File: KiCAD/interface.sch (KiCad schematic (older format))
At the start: 23 parts, among them M1 MANIFOLD, P10 C3SB, P11 VSel_Vlv, P14 X_VALVE, P17 PUMP, P18 Pump_Cable, P7 GAGE_PR, P9 C3SB, Q1 BCP5416TA, Q2 BCP5416TA, U1 TXB0104D

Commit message: work in progress
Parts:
- removed M1: MANIFOLD, symbol MANIFOLD
- added C14, C31: 100nF, uCm:c_0805, symbol C
- added D3, D9: S1D-13-F, uCm:diode-DO214AC, symbol D_1N4001
- added P34: VSel_Vlv2, uCm:Header_3, symbol CONN_3
- added P38: X_VALVE2, uCm:X_Valve_2, symbol X_VALVE
- added Q3, Q4: BCP5416TA, uCm:SOT223, symbol NPN_TIP112G
- added R6: 1k, uCm:r_0805, symbol R_10k
- added SP1: BUZZER, uCm:Speaker, symbol BUZZER
- C10, C11, C13, C17, C29, C7, C8, C9: footprint c_0805 -> uCm:c_0805
- C27: footprint C_ELCO_SMD -> uCm:C_ELCO_SMD
- D1: footprint diode-DO214AC -> uCm:diode-DO214AC
- P10, P9: footprint pin_strip_4-90 -> uCm:pin_strip_4-90
- P11: footprint Header_3 -> uCm:Header_3
- P14: footprint X_Valve_2 -> uCm:X_Valve_2
- P17: footprint Pump_P54E01R_02 -> uCm:Pump_P54E01R_02; symbol PUMP -> Pump
- P7: footprint HCEM500GUH9P3 -> uCm:HCEM500GUH9P3; symbol GAGE_PR -> Gage_Pr
- Q1, Q2: footprint SOT223 -> uCm:SOT223
- R4, R5: footprint r_0805 -> uCm:r_0805
- U1: footprint TXB0104D -> uCm:TXB0104D
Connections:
- net labels added: +Vlv2, -Vlv2, PD4_Valve2, Spk, ~PD6_Spk
- wire segments 100 -> 133
- no-connect marks 12 -> 8
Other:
- note added: "Speaker, 5V DC\ndigital PWM port ~PD6"
- note added: "Valve #2 on digital port PD4\neither 12V (V_IN) or 5V0"
- moved on the sheet: C13, D1, P11, P14, Q1

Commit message: layout, work in progress
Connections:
- net +Vlv: now also P14.2 (PM); no longer P14.1 (P1)
- net +Vlv2: now also P38.2 (PM); no longer P38.1 (P1)
- net -Vlv: now also P14.1 (P1); no longer P14.2 (PM)
- net -Vlv2: now also P38.1 (P1); no longer P38.2 (PM)
- net PD4_Valve2: now also Q1.1 (B); no longer Q3.1 (B)
- net ~PD5_Valve: now also Q3.1 (B); no longer Q1.1 (B)
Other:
- note added: "Valve #1 on digital port PD4\neither 12V (V_IN) or 5V0"
- note added: "Valve #2 on digital port PD5 [PWM]\neither 12V (V_IN) or 5V0"
- note removed: "Valve #1 on digital PWM port\neither 12V (V_IN) or 5V0"
- note removed: "Valve #2 on digital port PD4\neither 12V (V_IN) or 5V0"
- moved on the sheet: C13, C14, C31, D1, D3, D9, P11, P14, P34, P38, Q1, Q3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

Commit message: layout, work in progress
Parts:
- removed P17: PUMP, uCm:Pump_P54E01R_02, symbol Pump
- added P17: PUMP, uCm:Pump_P54E01R_02, symbol CONN_5
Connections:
- net 12V: now also P17.2
- net Pump: now also P17.4
- net Pump_Ret: now reaches C17.2, C27.2 (-), C29.2, Q2.2 (C)
- net Pump_Ret: now also P17.1
- no-connect marks 8 -> 7
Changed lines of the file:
@@
-$EndComp
-$Comp
-L Pump P17
-U 1 1 50E2B32E
-P 4600 5600
-F 0 "P17" V 4550 5600 40  0000 C CNN
-F 1 "PUMP" V 4650 5600 40  0000 C CNN
-F 2 "uCm:Pump_P54E01R_02" V 4750 5600 60  0001 C CNN
-F 3 "" H 4600 5600 60  0001 C CNN
-F 4 "http://www.xavitech.com/products" H 4600 6400 60  0001 L CNN "Field11"
-	1    4600 5600
-	1    0    0    -1
 $EndComp
 $Comp
@@
 	4000 5650 4000 6275
 NoConn ~ 4250 5750
-NoConn ~ 4250 5850
 Wire Notes Line
 	5575 7100 5575 5200
@@
 Text HLabel 8900 1200 0    40   Input ~ 0
 SDA
+Text Label 3250 6925 0    40   ~ 0
+Pump_Ret
+$Comp
+L CONN_5 P17
+U 1 1 55E98293
+P 4600 5550
+F 0 "P17" V 4550 5550 40  0000 C CNN
+F 1 "PUMP" V 4650 5550 40  0000 C CNN
+F 2 "uCm:Pump_P54E01R_02" H 4600 5500 60  0001 C CNN
+F 3 "http://www.xavitech.com/products" H 4600 5500 60  0001 C CNN
+	1    4600 5550
+	1    0    0    -1
+$EndComp
 $EndSCHEMATC

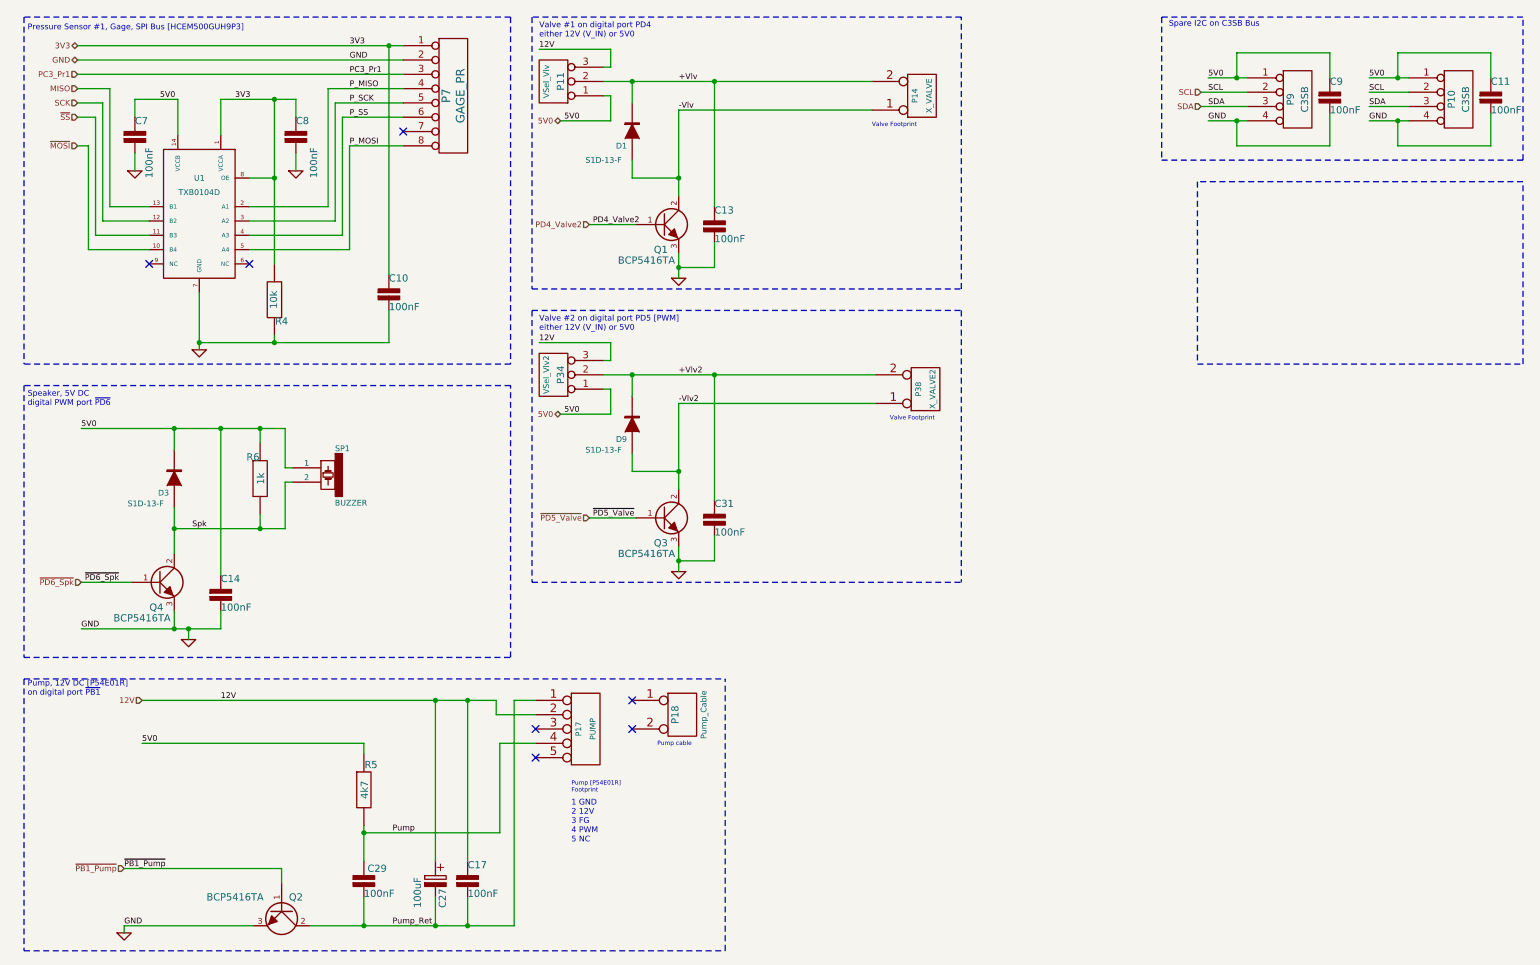
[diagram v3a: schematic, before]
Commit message: changed power supply section
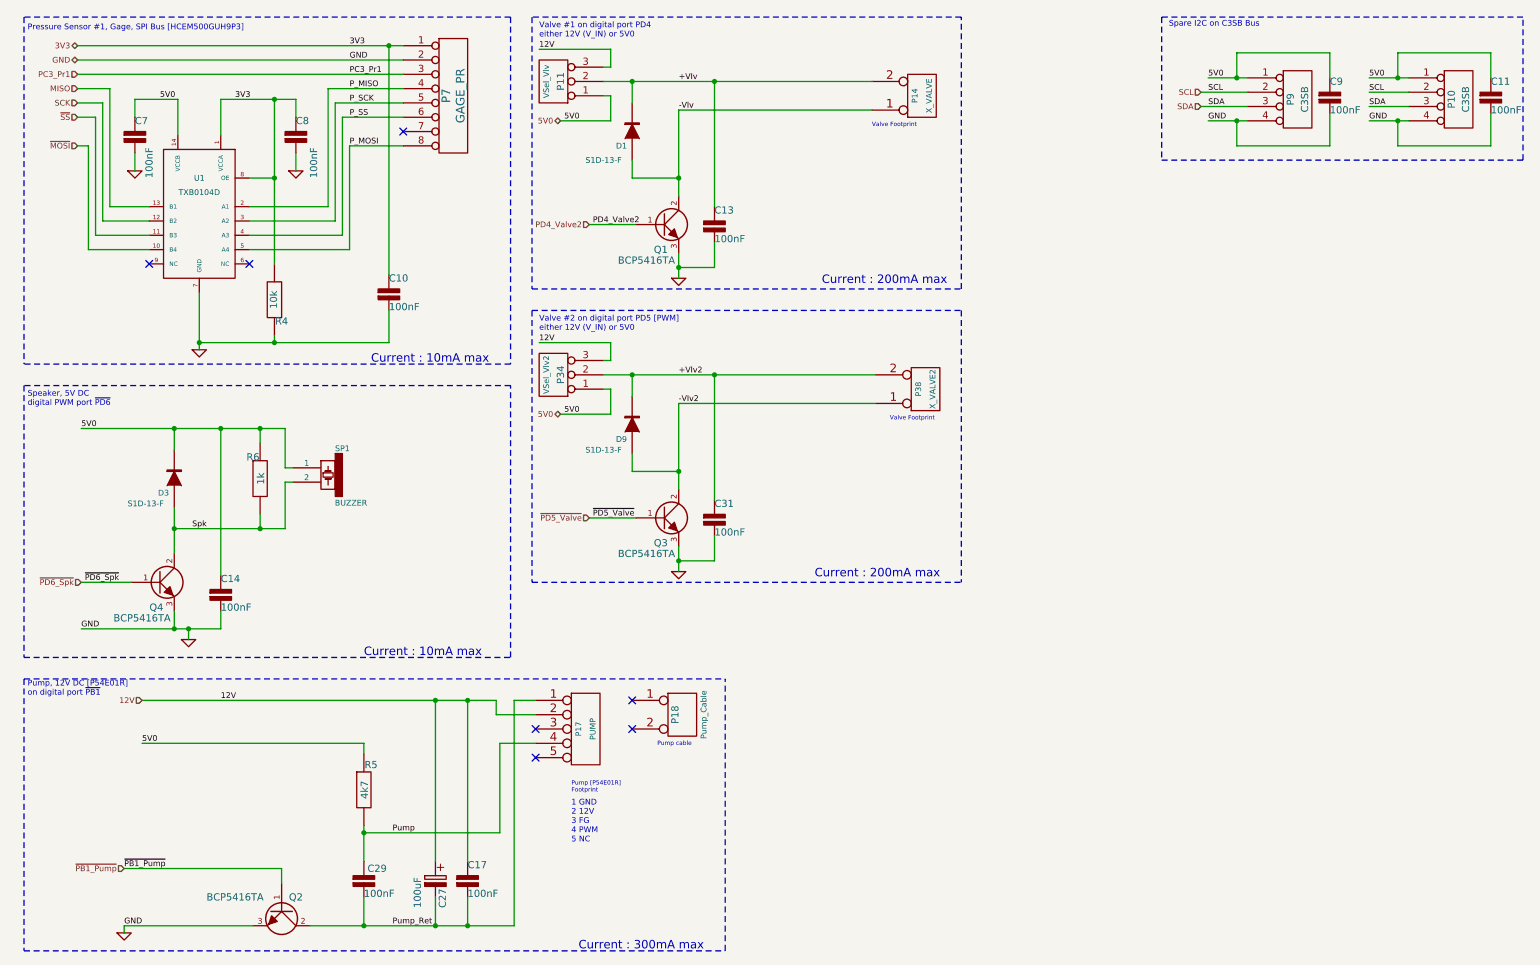
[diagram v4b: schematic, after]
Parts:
- C10, C11, C13, C14, C17, C29, C31, C7, C8, C9: Field10 399-5863-ND -> (none); Field11 http://www.digikey.com/product-detail/en/R82DC3100AA50J/399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 -> (none); Field4 CAP FILM 0.1UF 63VDC RADIAL -> (none); Field5 100nF, 63V -> (none); Field6 R82 -> (none); Field7 Kemet -> (none); Field8 R82DC3100AA50J -> (none); Field9 Digikey -> (none); manf# (none) -> CL21B104KCC5PNC
- C27: Field10 P833-ND -> (none); Field11 http://www.digikey.com/product-detail/en/ECE-A1CKA101/P833-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 -> (none); Field4 CAP ALUM 100UF 16V 20% RADIAL -> (none); Field5 100u,16V -> (none); Field6 Radial, Can, 6.3mm dia -> (none); Field7 Panasonic Electronic Components -> (none); Field8 ECE-A1CKA101 -> (none); Field9 Digikey -> (none); manf# (none) -> UWT1V101MCL1GS
- D1, D3, D9: Field10 1N4001FSCT-ND -> (none); Field11 http://www.digikey.com/product-detail/en/1N4001/1N4001FSCT-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 -> (none); Field4 DIODE GEN PURPOSE 50V 1A DO41 -> (none); Field5 50V, 1A -> (none); Field6 DO-204AL, DO-41, Axial -> (none); Field7 Fairchild Semiconductor -> (none); Field8 1N4001 -> (none); Field9 Digikey -> (none); manf# (none) -> S1D-13-F
- P10: manf# (none) -> PREC004SAAN-RC
- P11, P34: manf# (none) -> PREC003SAAN-RC
- P14, P38: Field10 X-1-05-S-F -> (none); Field11 http://ph.parker.com/webapp/wcs/stores/servlet/Product2_101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 -> (none); Field4 Miniature Pneumatic Solenoid Valve -> (none); Field5 3 Port, Direct-acting poppet style -> (none); Field6 8mm Solenoid Valve -> (none); Field7 Parker Hannifin Corporation -> (none); Field8 X-1-05-S-F -> (none); Field9 Parker Hannifin Corporation -> (none); manf# (none) -> X-1-05-S-F
- P17: manf# (none) -> P54E01R
- P7: Field10 HCEM500GUH9P3 -> (none); Field11 http://www.sensortechnics.com/en/products/pressure-sensors-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 -> (none); Field4 Miniature amplified pressure sensor -> (none); Field5 HCE Series -> (none); Field6 SMD single port, barbed port -> (none); Field7 SensorTechnics -> (none); Field8 HCEM500GUH9P3 -> (none); Field9 SensorTechnics -> (none); manf# (none) -> HCEM500GUH9P3
- P9: Field10 609-3317-ND -> (none); Field11 http://www.digikey.com/product-detail/en/68016-116HLF/609-3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 -> (none); Field4 CONN HEADER 16POS .100 R/A 30AU -> (none); Field5 Header, Unshrouded, Male pin, -> (none); Field6 0.1\" right angle -> (none); Field7 FCI -> (none); Field8 68016-116HLF -> (none); Field9 Digikey -> (none); manf# (none) -> PREC004SAAN-RC
- Q1, Q2, Q3, Q4: Field10 TIP112GOS-ND -> (none); Field11 http://www.digikey.com/scripts/dksearch/dksus.dll?vendor=0&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 -> (none); Field4 TRANS DARL NPN 2A 100V TO220AB -> (none); Field5 2A, 100V, 2W -> (none); Field6 TO-220-3 -> (none); Field7 ON Semiconductor -> (none); Field8 TIP112G -> (none); Field9 Digikey -> (none); manf# (none) -> BCP5416TA
- R4: Field10 CF18JT10K0CT-ND -> (none); Field11 http://www.digikey.com/product-detail/en/CF18JT10K0/CF18JT1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 -> (none); Field4 RES 10K OHM 1/8W 5% CF AXIAL -> (none); Field5 0.125W, 1/8W -> (none); Field6 Axial -> (none); Field7 Stackpole Electronics Inc -> (none); Field8 CF18JT10K0 -> (none); Field9 Digikey -> (none); manf# (none) -> RMCF0805JT10K0
- R5: Field10 CF18JT10K0CT-ND -> (none); Field11 http://www.digikey.com/product-detail/en/CF18JT10K0/CF18JT1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 -> (none); Field4 RES 10K OHM 1/8W 5% CF AXIAL -> (none); Field5 0.125W, 1/8W -> (none); Field6 Axial -> (none); Field7 Stackpole Electronics Inc -> (none); Field8 CF18JT10K0 -> (none); Field9 Digikey -> (none); manf# (none) -> RMCF0805JT4K70
- R6: Field10 CF18JT10K0CT-ND -> (none); Field11 http://www.digikey.com/product-detail/en/CF18JT10K0/CF18JT1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 -> (none); Field4 RES 10K OHM 1/8W 5% CF AXIAL -> (none); Field5 0.125W, 1/8W -> (none); Field6 Axial -> (none); Field7 Stackpole Electronics Inc -> (none); Field8 CF18JT10K0 -> (none); Field9 Digikey -> (none); manf# (none) -> RMCF0805JT1K00
- SP1: manf# (none) -> PS1240P02BT
- U1: Field10 296-21928-1-ND -> (none); Field11 http://www.digikey.com/product-detail/en/TXB0104DR/296-2192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 -> (none); Field4 IC VOLT-LEVEL TRANSLATOR 14-SOIC -> (none); Field5 Translator, Bidirectional -> (none); Field6 14-SOIC (0.154\", 3.90mm Width) -> (none); Field7 Texas Instruments -> (none); Field8 TXB0104DR -> (none); Field9 Digikey -> (none); manf# (none) -> TXB0104DR
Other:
- note added: "Current : 10mA max"
- note added: "Current : 200mA max"
- note added: "Current : 300mA max"

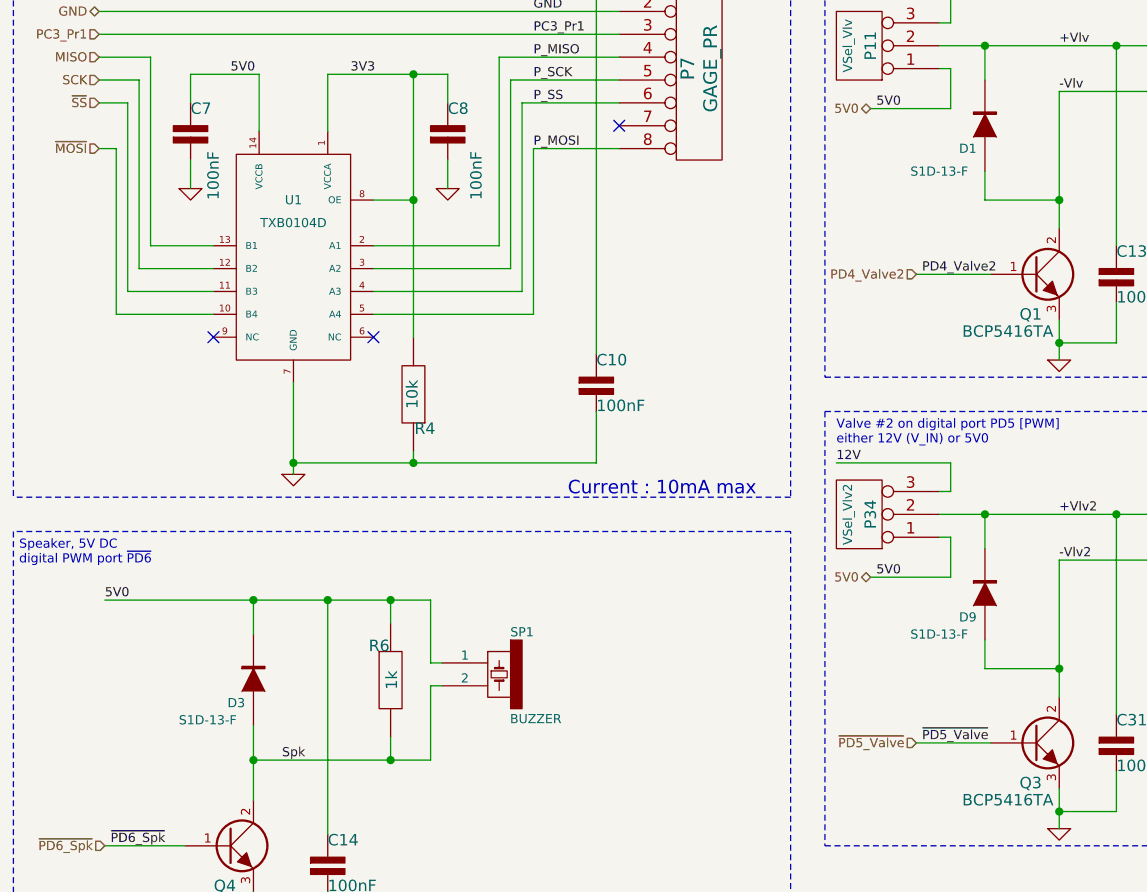
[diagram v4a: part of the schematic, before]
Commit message: changed power supply section
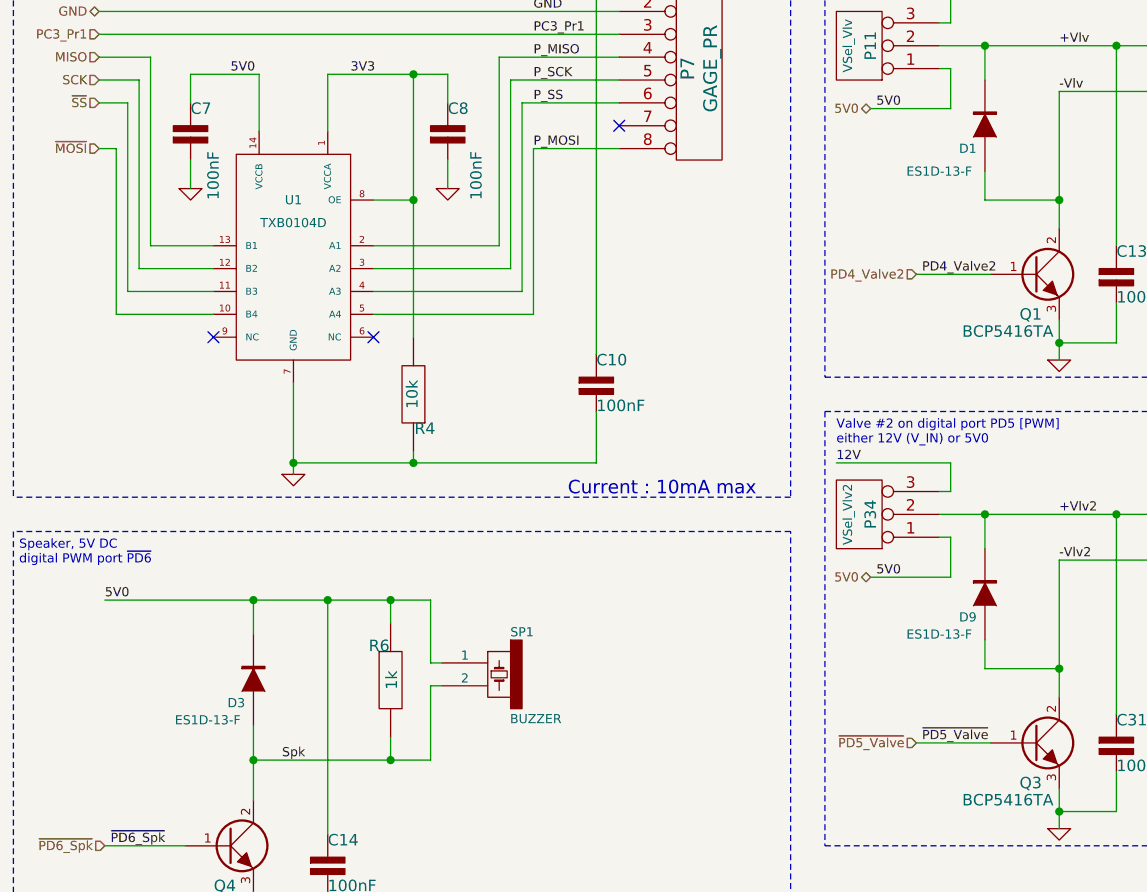
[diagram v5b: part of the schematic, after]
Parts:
- C27: footprint uCm:C_ELCO_SMD -> uCm:C_ELCO_SMD_6x8
- D1, D3, D9: value S1D-13-F -> ES1D-13-F; footprint uCm:diode-DO214AC -> uCm:Diode-SMA; manf# S1D-13-F -> ES1D-13-F
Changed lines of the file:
@@
 F 0 "C27" V 3600 6350 50  0000 L CNN
 F 1 "100uF" V 3425 6350 50  0000 L CNN
-F 2 "uCm:C_ELCO_SMD" H 3150 6550 50  0001 C CNN
+F 2 "uCm:C_ELCO_SMD_6x8" H 3150 6550 50  0001 C CNN
 F 3 "" H 3550 6575 60  0001 C CNN
 F 4 "UWT1V101MCL1GS" V 3550 6575 60  0001 C CNN "manf#"
@@
 P 4925 1375
 F 0 "D1" V 4825 1450 40  0000 C CNN
-F 1 "S1D-13-F" V 4725 1575 40  0000 C CNN
-F 2 "uCm:diode-DO214AC" V 4850 1525 40  0001 C CNN
+F 1 "ES1D-13-F" V 4725 1575 40  0000 C CNN
+F 2 "uCm:Diode-SMA" V 4850 1525 40  0001 C CNN
 F 3 "" H 4925 1375 60  0001 C CNN
-F 4 "S1D-13-F" V 4925 1375 60  0001 C CNN "manf#"
+F 4 "ES1D-13-F" V 4925 1375 60  0001 C CNN "manf#"
 	1    4925 1375
 	0    -1   -1   0
@@
 P 4925 3425
 F 0 "D9" V 4825 3500 40  0000 C CNN
-F 1 "S1D-13-F" V 4750 3625 40  0000 C CNN
-F 2 "uCm:diode-DO214AC" V 4850 3575 40  0001 C CNN
+F 1 "ES1D-13-F" V 4750 3625 40  0000 C CNN
+F 2 "uCm:Diode-SMA" V 4850 3575 40  0001 C CNN
 F 3 "" H 4925 3425 60  0001 C CNN
-F 4 "S1D-13-F" V 4925 3425 60  0001 C CNN "manf#"
+F 4 "ES1D-13-F" V 4925 3425 60  0001 C CNN "manf#"
 	1    4925 3425
 	0    -1   -1   0
@@
 P 1725 3800
 F 0 "D3" V 1625 3875 40  0000 C CNN
-F 1 "S1D-13-F" V 1550 4000 40  0000 C CNN
-F 2 "uCm:diode-DO214AC" V 1650 3950 40  0001 C CNN
+F 1 "ES1D-13-F" V 1550 4000 40  0000 C CNN
+F 2 "uCm:Diode-SMA" V 1650 3950 40  0001 C CNN
 F 3 "" H 1725 3800 60  0001 C CNN
-F 4 "S1D-13-F" V 1725 3800 60  0001 C CNN "manf#"
+F 4 "ES1D-13-F" V 1725 3800 60  0001 C CNN "manf#"
 	1    1725 3800
 	0    -1   -1   0
